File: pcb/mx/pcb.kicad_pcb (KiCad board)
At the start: 2 copper layers, 321 x 92.3 mm, 174 parts, among them SW1 Switch, SW10 Switch, SW11 Switch, SW12 Switch, SW13 Switch, SW14 Switch, SW15 Switch, SW16 Switch, SW17 Switch, SW18 Switch, SW19 Switch, SW2 Switch, SW20 Switch, SW21 Switch, SW22 Switch, SW23 Switch, SW24 Switch, SW25 Switch, SW26 Switch, SW27 Switch, SW28 Switch, SW29 Switch, SW3 Switch, SW30 Switch, SW31 Switch, SW32 Switch, SW33 Switch, SW34 Switch, SW35 Switch, SW36 Switch, SW37 Switch, SW38 Switch, SW4 Switch, SW5 Switch, SW6 Switch, SW7 Switch, SW8 Switch, SW9 Switch

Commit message: small updated
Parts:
- removed the REF** at (204.0, 97.5)
- removed the REF** at (153.0, 97.5)
- added REF**: Logo_stront-small, zzkeeb:Logo_stront-small, F.Cu at (204.5, 97.5)
- added REF**: Logo_stront-small, zzkeeb:Logo_stront-small, B.Cu at (153.5, 99.5)
- moved REF** 1.12 mm to (204.5, 99.5)
- moved REF** 0.50 mm to (153.5, 97.5)
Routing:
- net LED_r: track 127.1 -> 129.6 mm
- net RX_r: track 75.0 -> 77.2 mm
- net MOSI/SCL_r: track 124.8 -> 123.2 mm
- net SCLK/SDA_r: track 115.7 -> 114.1 mm
- net RST: track 71.8 -> 72.6 mm
- net CS: track 71.8 -> 72.6 mm
- net SCLK/SDA: track 95.4 -> 96.2 mm
- net MOSI/SCL: track 117.8 -> 118.6 mm
- net MISO: track 72.5 -> 73.4 mm
- net row0_r: track 266.2 -> 265.5 mm
- net row1_r: track 211.0 -> 210.3 mm
- net row3_r: track 258.8 -> 258.1 mm
- net BL_r: track 45.7 -> 45.0 mm
- net RST_r: track 99.4 -> 98.7 mm
- net 5V_VIK_r: track 120.5 -> 119.8 mm
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
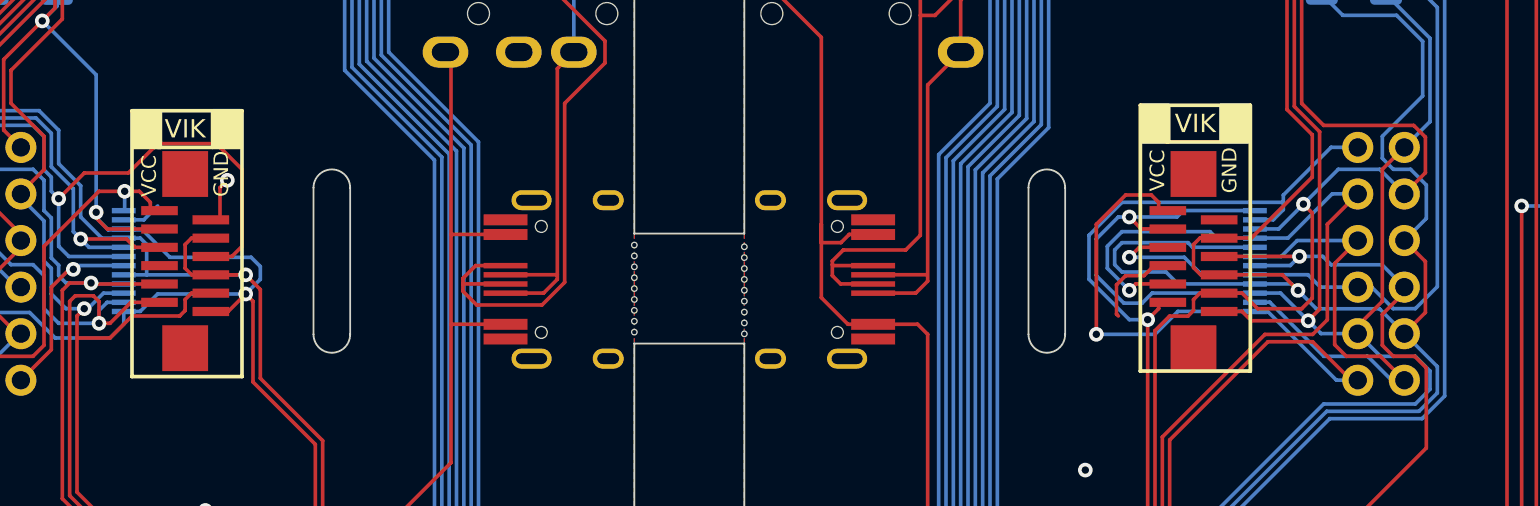
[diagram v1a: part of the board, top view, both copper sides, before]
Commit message: update components
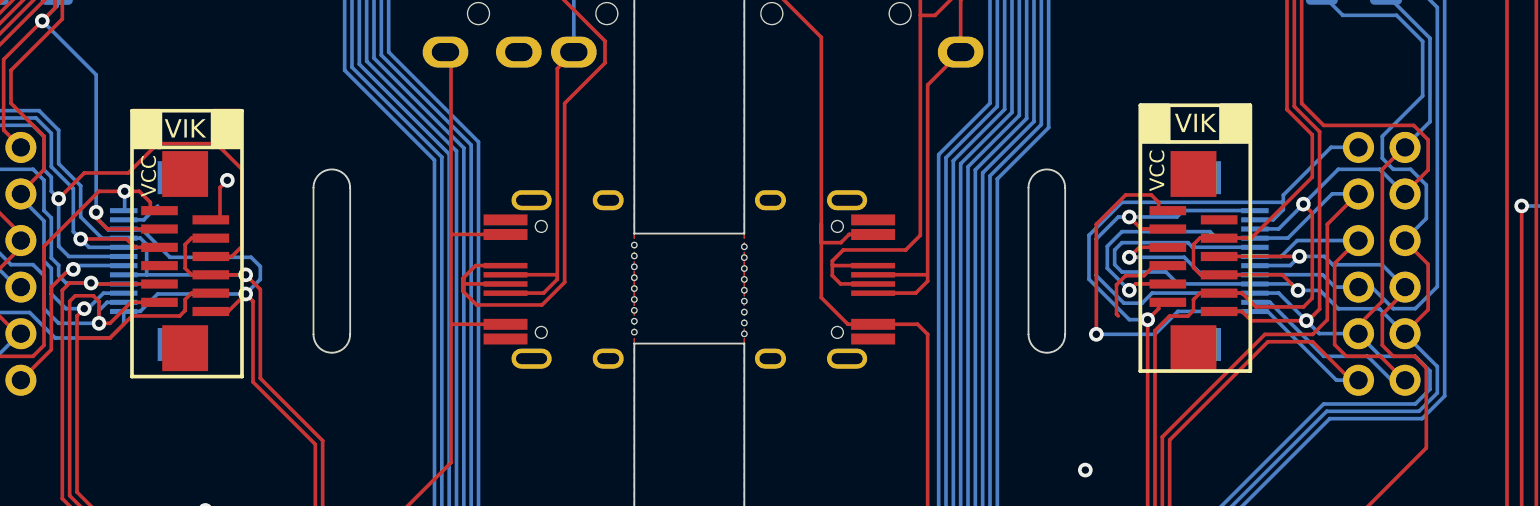
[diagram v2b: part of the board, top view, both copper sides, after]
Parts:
- VIK_K1, VIK_K4: footprint zzkeeb:Connector_FFC-FPC-vertical-12pin -> zzkeeb:Connector_VIK-vertical-keyboard
- VIK_K2: footprint zzkeeb:Connector_FPC-FFC-adapter-12pin -> zzkeeb:Connector_VIK-adapter-keyboard
- VIK_K3, VIK_K6: footprint Connector_FFC-FPC:Hirose_FH12-12S-0.5SH_1x12-1MP_P0.50mm_Horizontal -> zzkeeb:Connector_VIK-horizontal-keyboard
- VIK_K5: footprint zzkeeb:Connector_FPC-FFC-adapter-12pin -> zzkeeb:Connector_VIK-adapter-keyboard; moved to F.Cu
- moved VIK_K3 1.00 mm to (151.0, 111.5)
- moved VIK_K6 1.00 mm to (207.0, 111.5)
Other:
- board text removed: "VIK"
